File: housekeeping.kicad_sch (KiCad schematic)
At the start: 5 parts, among them U4 TPS7B8133QDGNRQ1

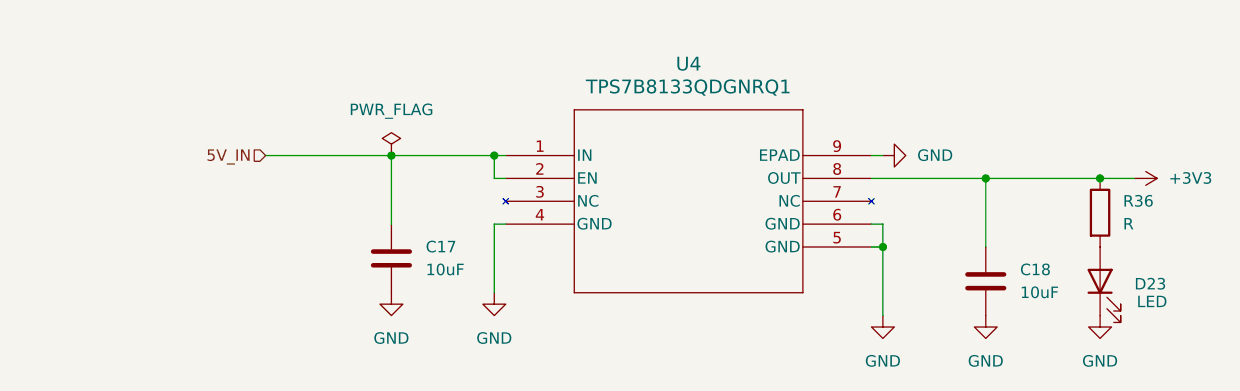
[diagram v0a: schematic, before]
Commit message: Adding in signals and cleaning up schematic
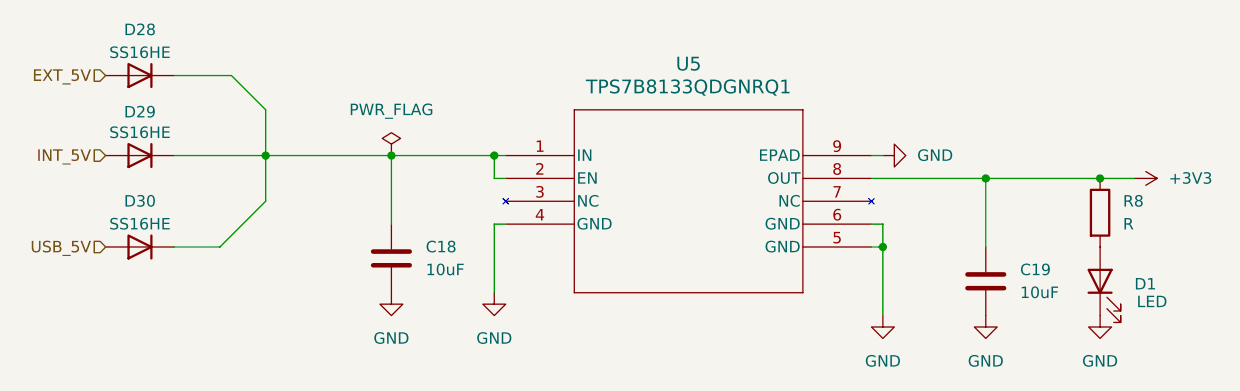
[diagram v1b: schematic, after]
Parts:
- removed D23: LED, symbol Device:LED
- removed R36: R, symbol Device:R
- added D1: LED, LED_SMD:LED_0603_1608Metric, symbol Device:LED
- added D28, D29, D30: SS16HE, Diode_SMD:D_SOD-323F, symbol Device:D
- added R8: R, Resistor_SMD:R_0603_1608Metric, symbol Device:R
- renumbered C17 to C18, C18 to C19, U4 to U5
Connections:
- net +3V3: now also R8.1
- net GND: now also D1.1 (K)
- net 5V_IN: no longer names the net of C18.1, U5.1 (IN), U5.2 (EN)
- net 5V_IN: now also D28.1 (K), D29.1 (K), D30.1 (K)
- new net: D1.2 (A), R8.2
- new net EXT_5V: D28.2 (A)
- new net INT_5V: D29.2 (A)
- new net USB_5V: D30.2 (A)

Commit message: prepaing for production
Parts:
- C18, C19: Supplier_2 (none) -> JLCPCB; Supplier_2 P/N (none) -> C440198
- D6: renamed from D28; Supplier_2 (none) -> JLCPCB; Supplier_2 P/N (none) -> C556433
- D7: renamed from D29; Supplier_2 (none) -> JLCPCB; Supplier_2 P/N (none) -> C556433
- D8: renamed from D30; Supplier_2 (none) -> JLCPCB; Supplier_2 P/N (none) -> C556433
- D9: renamed from D1; Mfr (none) -> ROHM Semi; Mfr P/N (none) -> SML-E12P8WT86; Supplier_2 (none) -> JLCPCB; Supplier_2 P/N (none) -> C126319
- R22: renamed from R8; value R -> 1k; Mfr (none) -> YAGEO; Mfr P/N (none) -> AC0603FR-071KL; Supplier_2 (none) -> JLCPCB; Supplier_2 P/N (none) -> C116692
- renumbered U5 to U4
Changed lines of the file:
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@@
 		(dnp no)
 		(fields_autoplaced yes)
-		(property "Reference" "#PWR067"
+		(property "Reference" "#PWR065"
 			(at 193.04 123.19 0)
 			(effects
@@
 			(project "BMS"
 				(path "/124184ba-5d68-4d9f-8da6-acc6720ab30b/93f9b420-7cce-46a9-9201-666f07a18f85/1875dae8-5675-4324-bc32-eabf0e306a05"
-					(reference "#PWR067")
+					(reference "#PWR065")
 					(unit 1)
 				)
@@
 		(dnp no)
 		(fields_autoplaced yes)
-		(property "Reference" "#PWR068"
+		(property "Reference" "#PWR066"
 			(at 193.04 101.6 0)
 			(effects
@@
 			(project "BMS"
 				(path "/124184ba-5d68-4d9f-8da6-acc6720ab30b/93f9b420-7cce-46a9-9201-666f07a18f85/1875dae8-5675-4324-bc32-eabf0e306a05"
-					(reference "#PWR068")
+					(reference "#PWR066")
 					(unit 1)
 				)
@@
 		(dnp no)
 		(fields_autoplaced yes)
-		(property "Reference" "#FLG03"
+		(property "Reference" "#FLG04"
 			(at 114.3 97.155 0)
 			(effects
@@
 			(project ""
 				(path "/124184ba-5d68-4d9f-8da6-acc6720ab30b/93f9b420-7cce-46a9-9201-666f07a18f85/1875dae8-5675-4324-bc32-eabf0e306a05"
-					(reference "#FLG03")
+					(reference "#FLG04")
 					(unit 1)
 				)
@@
 		(dnp no)
 		(fields_autoplaced yes)
-		(property "Reference" "#PWR064"
+		(property "Reference" "#PWR062"
 			(at 175.26 99.06 0)
 			(effects
@@
 			(project "BMS"
 				(path "/124184ba-5d68-4d9f-8da6-acc6720ab30b/93f9b420-7cce-46a9-9201-666f07a18f85/1875dae8-5675-4324-bc32-eabf0e306a05"
-					(reference "#PWR064")
+					(reference "#PWR062")
 					(unit 1)
 				)
@@
 		(dnp no)
 		(fields_autoplaced yes)
-		(property "Reference" "#PWR062"
+		(property "Reference" "#PWR060"
 			(at 114.3 120.65 0)
 			(effects
@@
 			(project ""
 				(path "/124184ba-5d68-4d9f-8da6-acc6720ab30b/93f9b420-7cce-46a9-9201-666f07a18f85/1875dae8-5675-4324-bc32-eabf0e306a05"
-					(reference "#PWR062")
+					(reference "#PWR060")
 					(unit 1)
 				)
@@
 		(dnp no)
 		(fields_autoplaced yes)
-		(property "Reference" "R8"
+		(property "Reference" "R22"
 			(at 195.58 104.1399 0)
 			(effects
@@
 			)
 		)
-		(property "Value" "R"
+		(property "Value" "1k"
 			(at 195.58 106.6799 0)
 			(effects
@@
 			)
 		)
-		(property "Description" "Resistor"
+		(property "Description" "100mW 1kΩ 75V Thick Film Resistor ±1% ±100ppm/℃ 0603"
 			(at 193.04 105.41 0)
 			(effects
@@
 			)
 		)
-		(property "Mfr" ""
+		(property "Mfr" "YAGEO"
 			(at 193.04 105.41 0)
 			(effects
@@
 			)
 		)
-		(property "Mfr P/N" ""
+		(property "Mfr P/N" "AC0603FR-071KL"
 			(at 193.04 105.41 0)
 			(effects
@@
 			)
 		)
-		(property "Supplier_2" ""
+		(property "Supplier_2" "JLCPCB"
 			(at 193.04 105.41 0)
 			(effects
@@
 			)
 		)
-		(property "Supplier_2 P/N" ""
+		(property "Supplier_2 P/N" "C116692"
 			(at 193.04 105.41 0)
 			(effects
@@
 		)
 		(property "Supplier_2 Price @ Qty" ""
+			(at 193.04 105.41 0)
+			(effects
+				(font
+					(size 1.27 1.27)
+				)
+				(hide yes)
+			)
+		)
+		(property "DigiKey_Part_Number" ""
 			(at 193.04 105.41 0)
 			(effects
@@
 			(project "BMS"
 				(path "/124184ba-5d68-4d9f-8da6-acc6720ab30b/93f9b420-7cce-46a9-9201-666f07a18f85/1875dae8-5675-4324-bc32-eabf0e306a05"
-					(reference "R8")
+					(reference "R22")
 					(unit 1)
 				)
@@
 		(dnp no)
 		(fields_autoplaced yes)
-		(property "Reference" "U5"
+		(property "Reference" "U4"
 			(at 147.32 88.9 0)
 			(effects
@@
 		)
 		(property "Supplier_2 Price @ Qty" "1"
+			(at 127 99.06 0)
+			(effects
+				(font
+					(size 1.27 1.27)
+				)
+				(hide yes)
+			)
+		)
+		(property "DigiKey_Part_Number" ""
 			(at 127 99.06 0)
 			(effects
@@
 			(project ""
 				(path "/124184ba-5d68-4d9f-8da6-acc6720ab30b/93f9b420-7cce-46a9-9201-666f07a18f85/1875dae8-5675-4324-bc32-eabf0e306a05"
-					(reference "U5")
+					(reference "U4")
 					(unit 1)
 				)
@@
 		(on_board yes)
 		(dnp no)
-		(property "Reference" "D28"
+		(property "Reference" "D6"
 			(at 86.36 85.09 0)
 			(effects
@@
 			)
 		)
-		(property "Supplier_2" ""
+		(property "Supplier_2" "JLCPCB"
 			(at 86.36 90.17 0)
 			(effects
@@
 			)
 		)
-		(property "Supplier_2 P/N" ""
+		(property "Supplier_2 P/N" "C556433"
 			(at 86.36 90.17 0)
 			(effects
@@
 		)
 		(property "Supplier_2 Price @ Qty" ""
+			(at 86.36 90.17 0)
+			(effects
+				(font
+					(size 1.27 1.27)
+				)
+				(hide yes)
+			)
+		)
+		(property "DigiKey_Part_Number" ""
 			(at 86.36 90.17 0)
 			(effects
@@
 			(project "BMS"
 				(path "/124184ba-5d68-4d9f-8da6-acc6720ab30b/93f9b420-7cce-46a9-9201-666f07a18f85/1875dae8-5675-4324-bc32-eabf0e306a05"
-					(reference "D28")
+					(reference "D6")
 					(unit 1)
 				)
@@
 		(on_board yes)
 		(dnp no)
-		(property "Reference" "D30"
+		(property "Reference" "D8"
 			(at 86.36 104.14 0)
 			(effects
@@
 			)
 		)
-		(property "Supplier_2" ""
+		(property "Supplier_2" "JLCPCB"
 			(at 86.36 109.22 0)
 			(effects
@@
 			)
 		)
-		(property "Supplier_2 P/N" ""
+		(property "Supplier_2 P/N" "C556433"
 			(at 86.36 109.22 0)
 			(effects
@@
 		)
 		(property "Supplier_2 Price @ Qty" ""
+			(at 86.36 109.22 0)
+			(effects
+				(font
+					(size 1.27 1.27)
+				)
+				(hide yes)
+			)
+		)
+		(property "DigiKey_Part_Number" ""
 			(at 86.36 109.22 0)
 			(effects
@@
 			(project "BMS"
 				(path "/124184ba-5d68-4d9f-8da6-acc6720ab30b/93f9b420-7cce-46a9-9201-666f07a18f85/1875dae8-5675-4324-bc32-eabf0e306a05"
-					(reference "D30")
+					(reference "D8")
 					(unit 1)
 				)
@@
 		(dnp no)
 		(fields_autoplaced yes)
-		(property "Reference" "#PWR063"
+		(property "Reference" "#PWR061"
 			(at 125.73 120.65 0)
 			(effects
@@
 			(project "BMS"
 				(path "/124184ba-5d68-4d9f-8da6-acc6720ab30b/93f9b420-7cce-46a9-9201-666f07a18f85/1875dae8-5675-4324-bc32-eabf0e306a05"
-					(reference "#PWR063")
+					(reference "#PWR061")
 					(unit 1)
 				)
@@
 			)
 		)
-		(property "Supplier_2" ""
+		(property "Supplier_2" "JLCPCB"
 			(at 114.3 110.49 0)
 			(effects
@@
 			)
 		)
-		(property "Supplier_2 P/N" ""
+		(property "Supplier_2 P/N" "C440198"
 			(at 114.3 110.49 0)
 			(effects
@@
 		)
 		(property "Supplier_2 Unit Price" ""
+			(at 114.3 110.49 0)
+			(effects
+				(font
+					(size 1.27 1.27)
+				)
+				(hide yes)
+			)
+		)
+		(property "DigiKey_Part_Number" ""
 			(at 114.3 110.49 0)
 			(effects
@@
 		(dnp no)
 		(fields_autoplaced yes)
-		(property "Reference" "#PWR066"
+		(property "Reference" "#PWR064"
 			(at 180.34 123.19 0)
 			(effects
@@
 			(project "BMS"
 				(path "/124184ba-5d68-4d9f-8da6-acc6720ab30b/93f9b420-7cce-46a9-9201-666f07a18f85/1875dae8-5675-4324-bc32-eabf0e306a05"
-					(reference "#PWR066")
+					(reference "#PWR064")
 					(unit 1)
 				)
@@
 			)
 		)
-		(property "Supplier_2" ""
+		(property "Supplier_2" "JLCPCB"
 			(at 180.34 113.03 0)
 			(effects
@@
 			)
 		)
-		(property "Supplier_2 P/N" ""
+		(property "Supplier_2 P/N" "C440198"
 			(at 180.34 113.03 0)
 			(effects
@@
 		)
 		(property "Supplier_2 Unit Price" ""
+			(at 180.34 113.03 0)
+			(effects
+				(font
+					(size 1.27 1.27)
+				)
+				(hide yes)
+			)
+		)
+		(property "DigiKey_Part_Number" ""
 			(at 180.34 113.03 0)
 			(effects
@@
 		(dnp no)
 		(fields_autoplaced yes)
-		(property "Reference" "#PWR065"
+		(property "Reference" "#PWR063"
 			(at 168.91 123.19 0)
 			(effects
@@
 			(project "BMS"
 				(path "/124184ba-5d68-4d9f-8da6-acc6720ab30b/93f9b420-7cce-46a9-9201-666f07a18f85/1875dae8-5675-4324-bc32-eabf0e306a05"
-					(reference "#PWR065")
+					(reference "#PWR063")
 					(unit 1)
 				)
@@
 		(on_board yes)
 		(dnp no)
-		(property "Reference" "D1"
+		(property "Reference" "D9"
 			(at 196.85 113.3474 90)
 			(effects
@@
 			)
 		)
-		(property "Description" "Light emitting diode"
+		(property "Description" ".2V 20mA 54mW 560nm 6.3mcd Common Cathode Green White"
 			(at 193.04 113.03 0)
 			(effects
@@
 			)
 		)
-		(property "Mfr" ""
+		(property "Mfr" "ROHM Semi"
 			(at 193.04 113.03 0)
 			(effects
@@
 			)
 		)
-		(property "Mfr P/N" ""
+		(property "Mfr P/N" "SML-E12P8WT86"
 			(at 193.04 113.03 0)
 			(effects
@@
 			)
 		)
-		(property "Supplier_2" ""
+		(property "Supplier_2" "JLCPCB"
 			(at 193.04 113.03 0)
 			(effects
@@
 			)
 		)
-		(property "Supplier_2 P/N" ""
+		(property "Supplier_2 P/N" "C126319"
 			(at 193.04 113.03 0)
 			(effects
@@
 		(property "Supplier_2 Price @ Qty" ""
 			(at 193.04 113.03 0)
+			(effects
+				(font
+					(size 1.27 1.27)
+				)
+				(hide yes)
+			)
+		)
+		(property "DigiKey_Part_Number" ""
+			(at 193.04 113.03 90)
 			(effects
 				(font
@@
 			(project "BMS"
 				(path "/124184ba-5d68-4d9f-8da6-acc6720ab30b/93f9b420-7cce-46a9-9201-666f07a18f85/1875dae8-5675-4324-bc32-eabf0e306a05"
-					(reference "D1")
+					(reference "D9")
 					(unit 1)
 				)
@@
 		(on_board yes)
 		(dnp no)
-		(property "Reference" "D29"
+		(property "Reference" "D7"
 			(at 86.36 94.234 0)
 			(effects
@@
 			)
 		)
-		(property "Supplier_2" ""
+		(property "Supplier_2" "JLCPCB"
 			(at 86.36 99.06 0)
 			(effects
@@
 			)
 		)
-		(property "Supplier_2 P/N" ""
+		(property "Supplier_2 P/N" "C556433"
 			(at 86.36 99.06 0)
 			(effects
@@
 		)
 		(property "Supplier_2 Price @ Qty" ""
+			(at 86.36 99.06 0)
+			(effects
+				(font
+					(size 1.27 1.27)
+				)
+				(hide yes)
+			)
+		)
+		(property "DigiKey_Part_Number" ""
 			(at 86.36 99.06 0)
 			(effects
@@
 			(project "BMS"
 				(path "/124184ba-5d68-4d9f-8da6-acc6720ab30b/93f9b420-7cce-46a9-9201-666f07a18f85/1875dae8-5675-4324-bc32-eabf0e306a05"
-					(reference "D29")
+					(reference "D7")
 					(unit 1)
 				)
